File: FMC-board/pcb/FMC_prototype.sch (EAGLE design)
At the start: 111 parts, among them Q1 SSM3J328R, U1 4901, U2 7933, U3 ADN4663, U4 ADN4663, U5 ADN4664, U6 PDS1, U7 4901, U8 FMC_SINGLE_WIDTH_MODULE

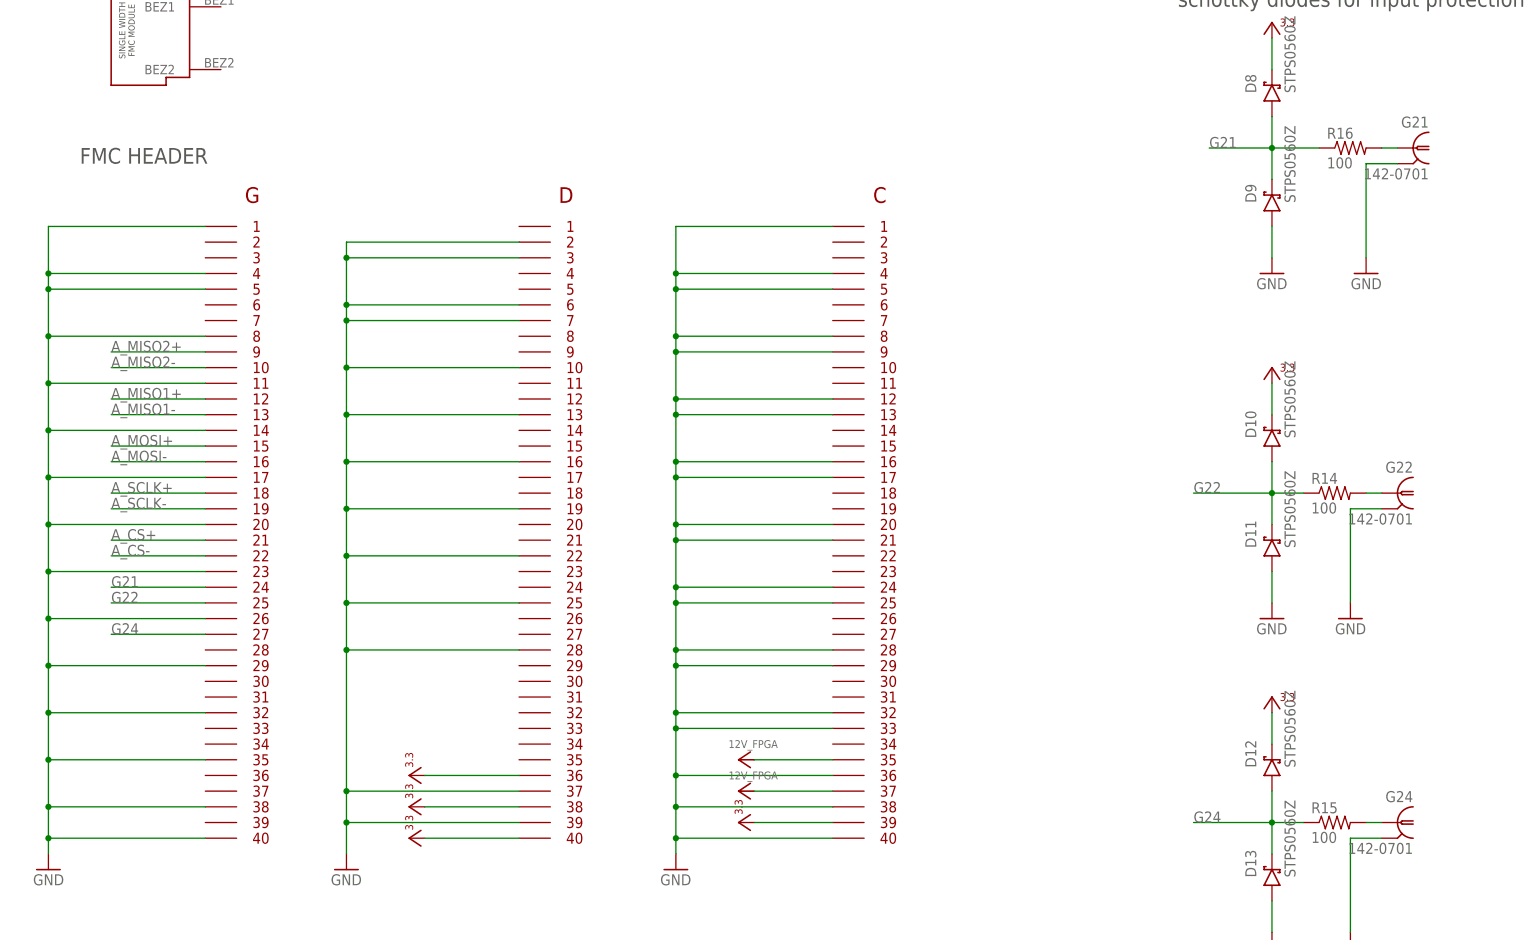
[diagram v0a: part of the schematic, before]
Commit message: Fixed SMA component names to match new FMC loctaions.
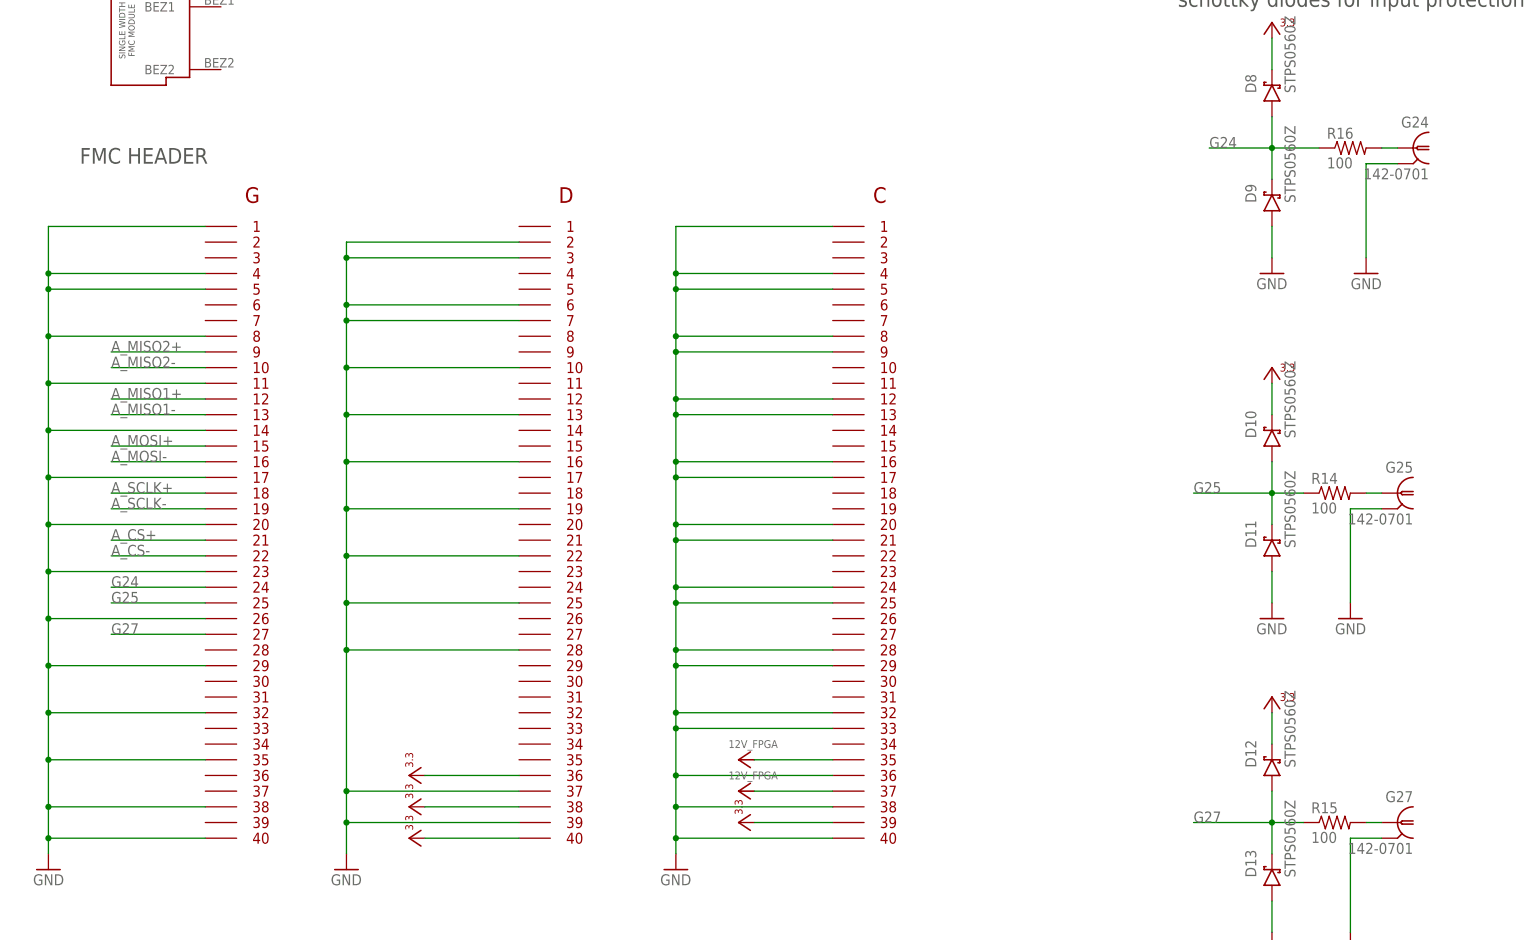
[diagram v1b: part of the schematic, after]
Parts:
- removed G21: 142-0701, jonnew:COAX_SMA-VERT
- added G27: 142-0701, jonnew:COAX_SMA-VERT
- renumbered G22 to G25
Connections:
- net G22 renamed G25
- removed net G21: D8.A, D9.C, FMCG$1.P$64, R16.1
- new net G27: D12.A, D13.C, FMCG$1.P$67, R15.1
- net G24: now also D8.A, D9.C, FMCG$1.P$64, R16.1; no longer D12.A, D13.C, FMCG$1.P$67, R15.1
- net GND: now also G27.2; no longer G21.2
- net N$19: now also G27.1; no longer G24.1
- net N$2: now also G24.1; no longer G21.1
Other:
- moved on the sheet: G24
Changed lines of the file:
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@@
 <part name="POW_SEL" library="jonnew" deviceset="JP3E" device=""/>
 <part name="POW_TP" library="jonnew" deviceset="JP3E" device=""/>
-<part name="G21" library="jonnew" deviceset="COAX" device="_SMA-VERT" value="142-0701"/>
-<part name="G22" library="jonnew" deviceset="COAX" device="_SMA-VERT" value="142-0701"/>
 <part name="G24" library="jonnew" deviceset="COAX" device="_SMA-VERT" value="142-0701"/>
+<part name="G25" library="jonnew" deviceset="COAX" device="_SMA-VERT" value="142-0701"/>
+<part name="G27" library="jonnew" deviceset="COAX" device="_SMA-VERT" value="142-0701"/>
 <part name="D8" library="jonnew" deviceset="S-DIODE" device="SOD-123" value="STPS0560Z"/>
 <part name="D9" library="jonnew" deviceset="S-DIODE" device="SOD-123" value="STPS0560Z"/>
@@
 <instance part="POW_SEL" gate="G$1" x="358.14" y="370.84"/>
 <instance part="POW_TP" gate="G$1" x="378.46" y="398.78" rot="R180"/>
-<instance part="G21" gate="G$1" x="612.14" y="175.26" rot="MR0"/>
-<instance part="G22" gate="G$1" x="609.6" y="119.38" rot="MR0"/>
-<instance part="G24" gate="G$1" x="609.6" y="66.04" rot="MR0"/>
+<instance part="G24" gate="G$1" x="612.14" y="175.26" rot="MR0"/>
+<instance part="G25" gate="G$1" x="609.6" y="119.38" rot="MR0"/>
+<instance part="G27" gate="G$1" x="609.6" y="66.04" rot="MR0"/>
 <instance part="D8" gate="G$1" x="589.28" y="185.42" rot="R90"/>
 <instance part="D9" gate="G$1" x="589.28" y="167.64" rot="R90"/>
@@
 </segment>
 <segment>
-<pinref part="G21" gate="G$1" pin="2"/>
+<pinref part="G24" gate="G$1" pin="2"/>
 <wire x1="609.6" y1="172.72" x2="604.52" y2="172.72" width="0.1524" layer="91"/>
 <pinref part="GND7" gate="1" pin="GND"/>
@@
 </segment>
 <segment>
-<pinref part="G22" gate="G$1" pin="2"/>
+<pinref part="G25" gate="G$1" pin="2"/>
 <pinref part="GND1" gate="1" pin="GND"/>
 <wire x1="607.06" y1="116.84" x2="601.98" y2="116.84" width="0.1524" layer="91"/>
@@
 </segment>
 <segment>
-<pinref part="G24" gate="G$1" pin="2"/>
+<pinref part="G27" gate="G$1" pin="2"/>
 <pinref part="GND22" gate="1" pin="GND"/>
 <wire x1="607.06" y1="63.5" x2="601.98" y2="63.5" width="0.1524" layer="91"/>
@@
 </segment>
 </net>
-<net name="G21" class="0">
+<net name="G24" class="0">
 <segment>
 <label x="401.32" y="104.14" size="1.778" layer="95"/>
@@
 </segment>
 </net>
-<net name="G22" class="0">
+<net name="G25" class="0">
 <segment>
 <label x="401.32" y="101.6" size="1.778" layer="95"/>
@@
 </segment>
 </net>
-<net name="G24" class="0">
+<net name="G27" class="0">
 <segment>
 <label x="401.32" y="96.52" size="1.778" layer="95"/>
@@
 <net name="N$2" class="0">
 <segment>
-<pinref part="G21" gate="G$1" pin="1"/>
+<pinref part="G24" gate="G$1" pin="1"/>
 <pinref part="R16" gate="R" pin="2"/>
 <wire x1="607.06" y1="175.26" x2="609.6" y2="175.26" width="0.1524" layer="91"/>
@@
 <net name="N$18" class="0">
 <segment>
-<pinref part="G22" gate="G$1" pin="1"/>
+<pinref part="G25" gate="G$1" pin="1"/>
 <pinref part="R14" gate="R" pin="2"/>
 <wire x1="604.52" y1="119.38" x2="607.06" y2="119.38" width="0.1524" layer="91"/>
@@
 <net name="N$19" class="0">
 <segment>
-<pinref part="G24" gate="G$1" pin="1"/>
+<pinref part="G27" gate="G$1" pin="1"/>
 <pinref part="R15" gate="R" pin="2"/>
 <wire x1="604.52" y1="66.04" x2="607.06" y2="66.04" width="0.1524" layer="91"/>

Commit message: Final changes to layout before fabrication
- Gerbers are being sent to Seeed for fabrication
- I will tag this Rev 0.1
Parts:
- U1, U7: device puggleboard:TPS7A4901DGNR -> jonnew:TPS7A4901DGNR
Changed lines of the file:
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@@
 <part name="C20" library="puggleboard" deviceset="C" device="_1206" value="10uF"/>
 <part name="C24" library="puggleboard" deviceset="C" device="_1206" value="10uF"/>
-<part name="U7" library="puggleboard" deviceset="TPS7A4901DGNR" device="" value="4901"/>
+<part name="U7" library="jonnew" deviceset="TPS7A4901DGNR" device="" value="4901"/>
 <part name="R12" library="jonnew" deviceset="R" device="_0603" value="20k"/>
 <part name="R13" library="jonnew" deviceset="R" device="_0603" value="10k"/>
@@
 <part name="C12" library="puggleboard" deviceset="C" device="_1206" value="10uF"/>
 <part name="C1" library="puggleboard" deviceset="C" device="_1206" value="10uF"/>
-<part name="U1" library="puggleboard" deviceset="TPS7A4901DGNR" device="" value="4901"/>
+<part name="U1" library="jonnew" deviceset="TPS7A4901DGNR" device="" value="4901"/>
 <part name="R5" library="jonnew" deviceset="R" device="_0603" value="20k"/>
 <part name="R6" library="jonnew" deviceset="R" device="_0603" value="10k"/>

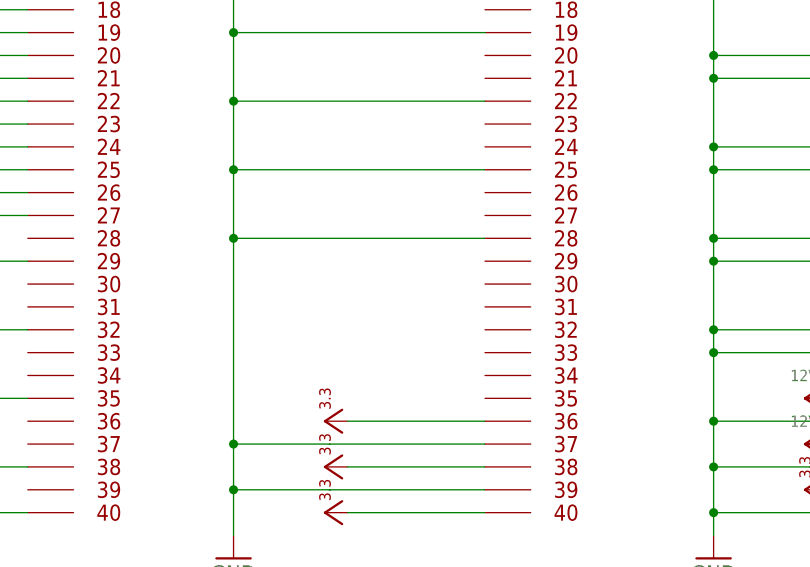
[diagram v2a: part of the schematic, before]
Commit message: Tied the TDI/TDO pins together on the FMC header.
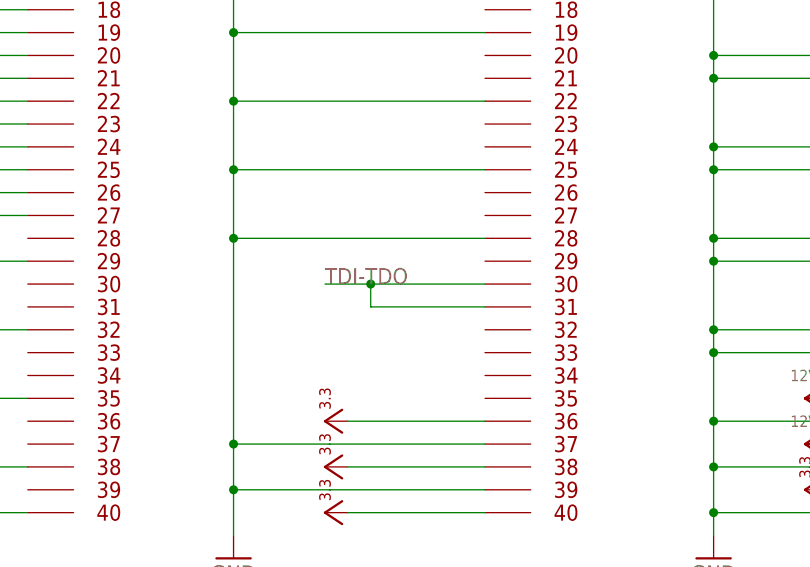
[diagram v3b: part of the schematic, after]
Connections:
- new net TDI-TDO: FMCG$1.P$110, FMCG$1.P$111
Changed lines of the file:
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@@
+</segment>
+</net>
+<net name="TDI-TDO" class="0">
+<segment>
+<pinref part="FMC" gate="G$1" pin="P$110"/>
+<wire x1="467.36" y1="88.9" x2="454.66" y2="88.9" width="0.1524" layer="91"/>
+<pinref part="FMC" gate="G$1" pin="P$111"/>
+<wire x1="454.66" y1="88.9" x2="449.58" y2="88.9" width="0.1524" layer="91"/>
+<wire x1="467.36" y1="86.36" x2="454.66" y2="86.36" width="0.1524" layer="91"/>
+<wire x1="454.66" y1="86.36" x2="454.66" y2="88.9" width="0.1524" layer="91"/>
+<junction x="454.66" y="88.9"/>
+<label x="449.58" y="88.9" size="1.778" layer="95"/>
 </segment>
 </net>
